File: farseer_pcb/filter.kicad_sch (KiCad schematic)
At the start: 17 parts, among them J2 UMC_JACK_SMD, U2 UAF42_SMA, U3 UAF42_SMA

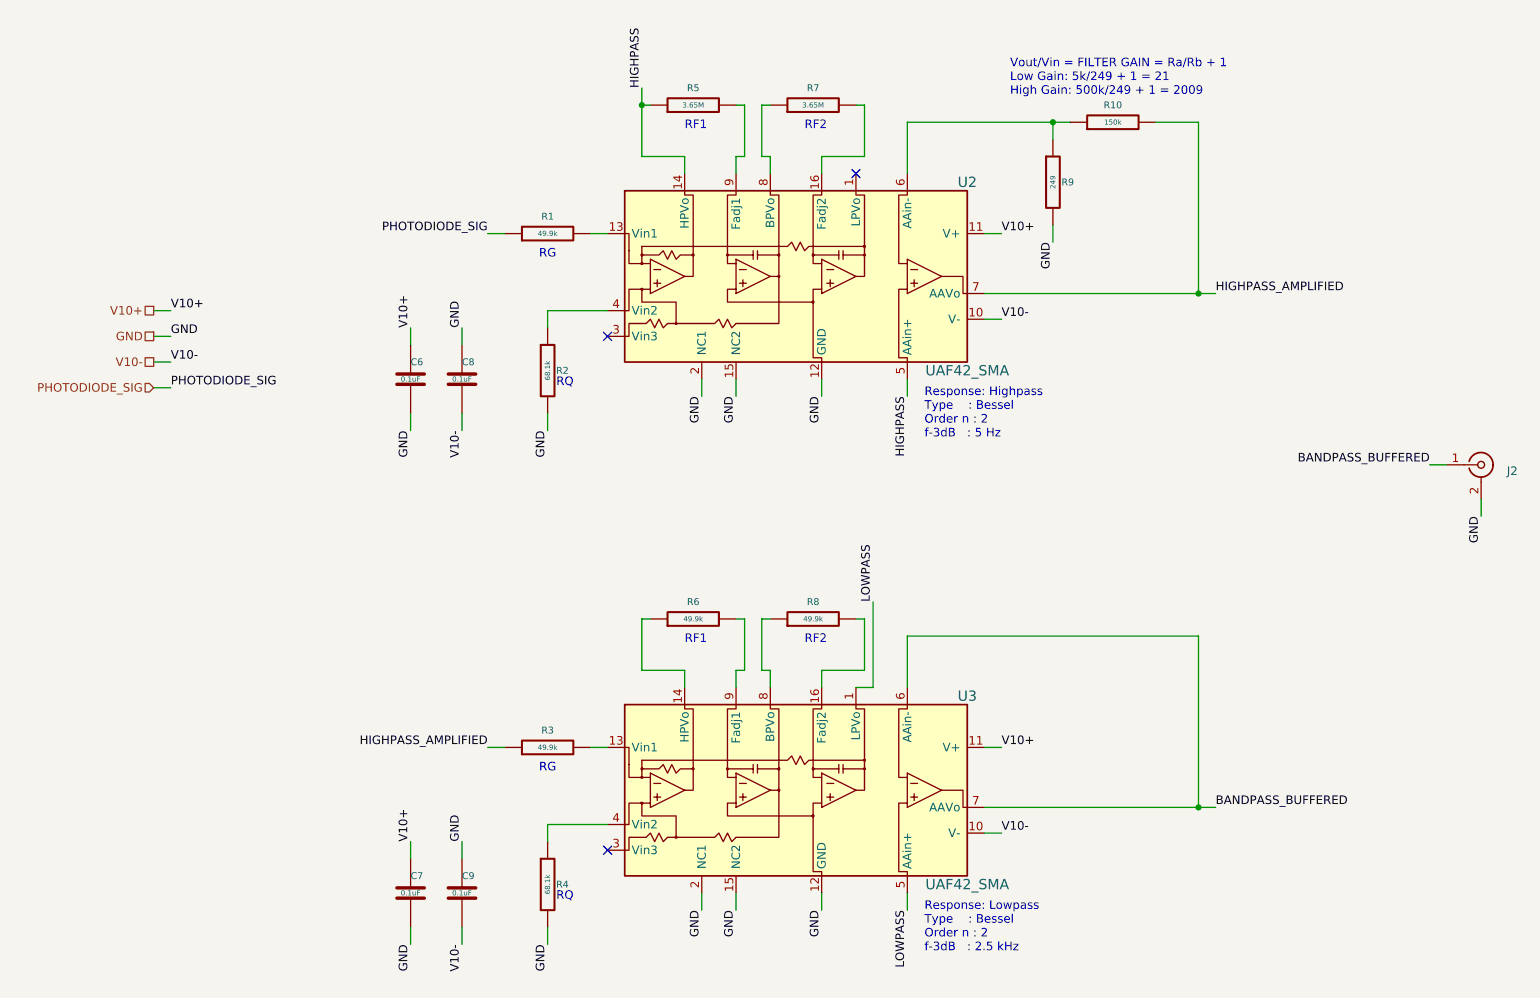
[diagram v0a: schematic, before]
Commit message: Begin board resize
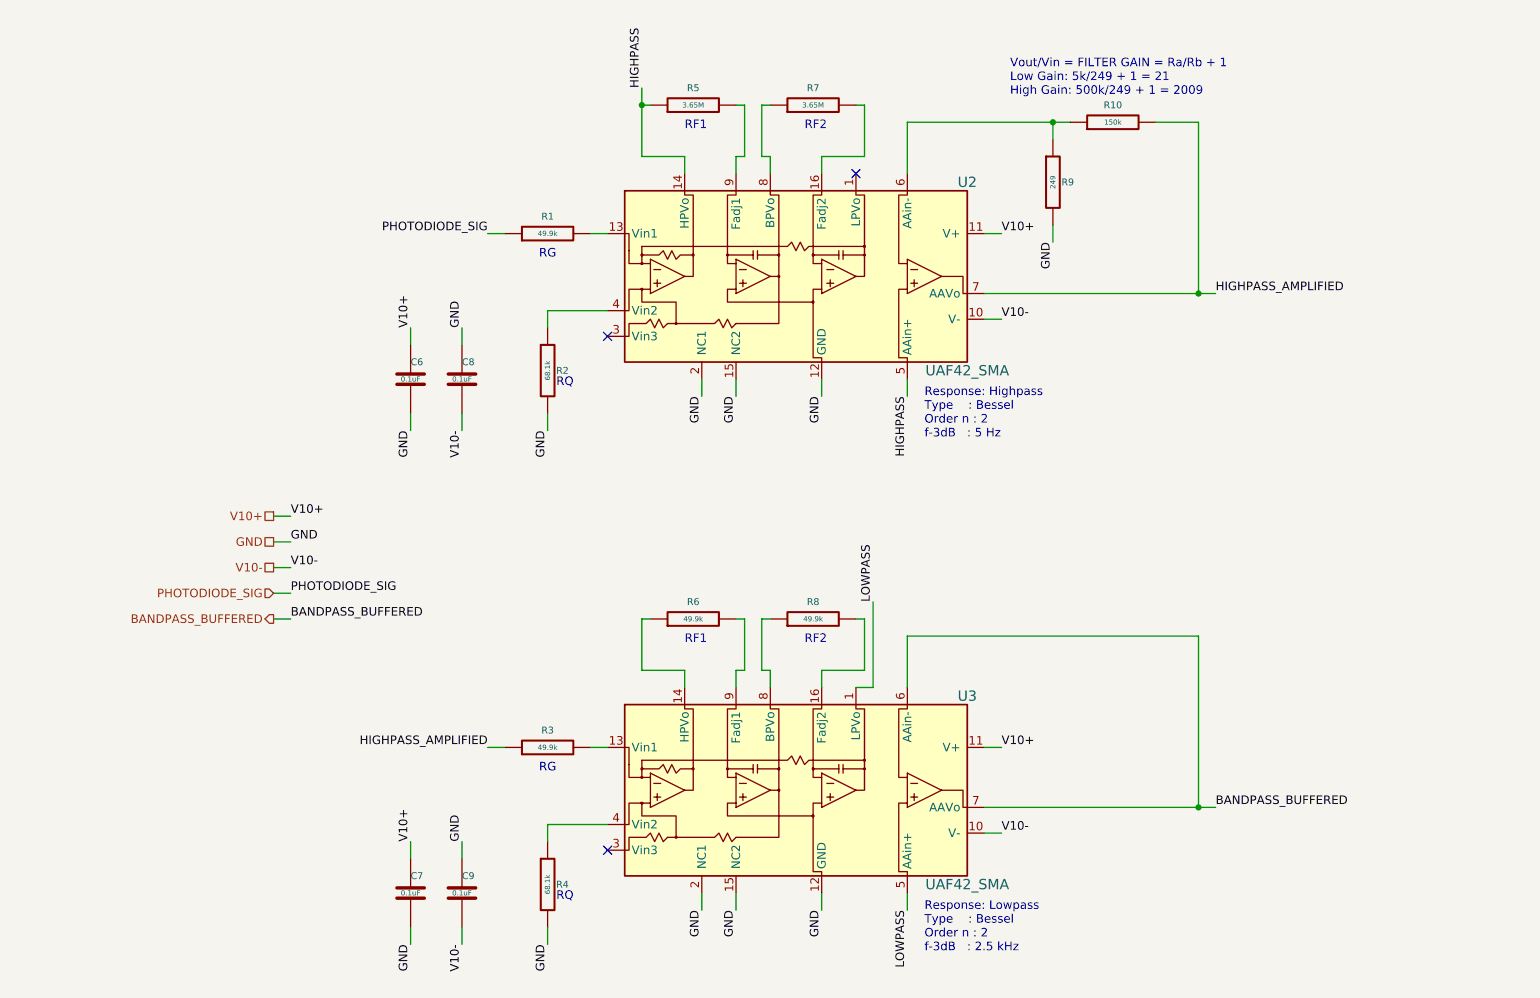
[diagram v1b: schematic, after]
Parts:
- removed J2: UMC_JACK_SMD, Janelia:UMC_AMPHENOL_A-1JB, symbol Janelia:CONN_UMC_JACK_SMD
- C6, C7, C8, C9: MFN Yageo -> (none); MPN CC0402ZRY5V8BB104 -> (none); Manufacturer (none) -> Yageo; Manufacturer Part Number (none) -> CC0402ZRY5V8BB104; Synopsis (none) -> CAP CER 0.1UF 25V Y5V
- R1, R3, R6, R8: MFN Panasonic Electronic Components -> (none); MPN ERJ-2RKF4992X -> (none); Manufacturer (none) -> Panasonic Electronic Components; Manufacturer Part Number (none) -> ERJ-2RKF4992X; Synopsis (none) -> RES SMD 49.9K OHM 1% 1/10W
- R10: MFN Panasonic Electronic Components -> (none); MPN ERA-8AEB154V -> (none); Manufacturer (none) -> Panasonic Electronic Components; Manufacturer Part Number (none) -> ERA-8AEB154V; Synopsis (none) -> RES SMD 150K OHM 0.1% 1/4W
- R2, R4: MFN Panasonic Electronic Components -> (none); MPN ERJ-2RKF6812X -> (none); Manufacturer (none) -> Panasonic Electronic Components; Manufacturer Part Number (none) -> ERJ-2RKF6812X; Synopsis (none) -> RES SMD 68.1K OHM 1% 1/10W
- R5, R7: MFN Vishay Dale -> (none); MPN CRCW06033M65FKEA -> (none); Manufacturer (none) -> Vishay Dale; Manufacturer Part Number (none) -> CRCW06033M65FKEA; Synopsis (none) -> RES SMD 3.65M OHM 1% 1/10W
- R9: MFN Panasonic Electronic Components -> (none); MPN ERJ-2RKF2490X -> (none); Manufacturer (none) -> Panasonic Electronic Components; Manufacturer Part Number (none) -> ERJ-2RKF2490X; Synopsis (none) -> RES SMD 249 OHM 1% 1/10W
- U2, U3: MFN Texas Instruments -> (none); MPN UAF42AU -> (none); Manufacturer (none) -> Texas Instruments; Manufacturer Part Number (none) -> UAF42AU; Synopsis (none) -> IC UNIV ACTIVE FILTER 16-SOIC
